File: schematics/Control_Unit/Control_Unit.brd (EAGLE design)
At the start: 49.8 x 49.8 mm, 282 parts, among them IC1 74HC174N, IC10 74HC74N, IC101 74HCT08N, IC102 74HC151N, IC103 74HC373N, IC104 74HCT08N, IC105 74HC151N, IC106 74HC151N, IC108 74HCT32N, IC109 74HCT08N, IC11 74HC74N, IC110 74HCT32N, IC111 74HC151N, IC112 74HCT32N, IC113 74HC151N, IC114 74HC151N, IC115 74HC151N, IC116 74HC373N, IC117 74HC74N, IC12 74AC08N, IC124 74HCT32N, IC125 74HCT08N, IC126 74AC157N, IC127 74HCT08N, IC128 74AC08N, IC129 74AC08N, IC13 74AC08N, IC130 74HCT04N, IC133 74HCT04N, IC134 74HCT08N, IC135 74HCT08N, IC136 74HCT08N, IC14 74HC74N, IC141 74HCT32N, IC15 74HC74N, IC16 74AC08N, IC164 74HC174N, IC165 74HC174N, IC166 74HC174N, IC167 74HC174N, IC168 74HCT32N, IC169 74HCT32N, IC17 74HCT32N, IC172 74HCT32N, IC173 74HCT32N, IC175 74HC193N, IC176 74HC193N, IC177 74HC193N, IC178 74HC193N, IC179 74HC193N, IC18 74AC08N, IC180 74HC193N, IC181 74HC193N, IC182 74HC193N, IC19 74AC08N, IC190 74HCT32N, IC191 74HCT32N, IC2 74HC174N, IC20 74AC08N, IC21 74AC08N, IC22 74HCT32N, IC23 74HCT08N, IC24 74HCT08N, IC25 74HCT32N, IC26 74HCT08N, IC27 74HCT08N, IC28 74HCT08N, IC29 74HCT32N, IC3 74HC151N, IC30 74HCT08N, IC31 74HC74N, IC32 74HCT32N, IC33 74HCT32N, IC34 74HCT08N, IC35 74HCT04N, IC36 74HCT32N, IC38 74HCT08N, IC39 74HCT08N, IC4 74HC174N, IC40 74ACT157N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

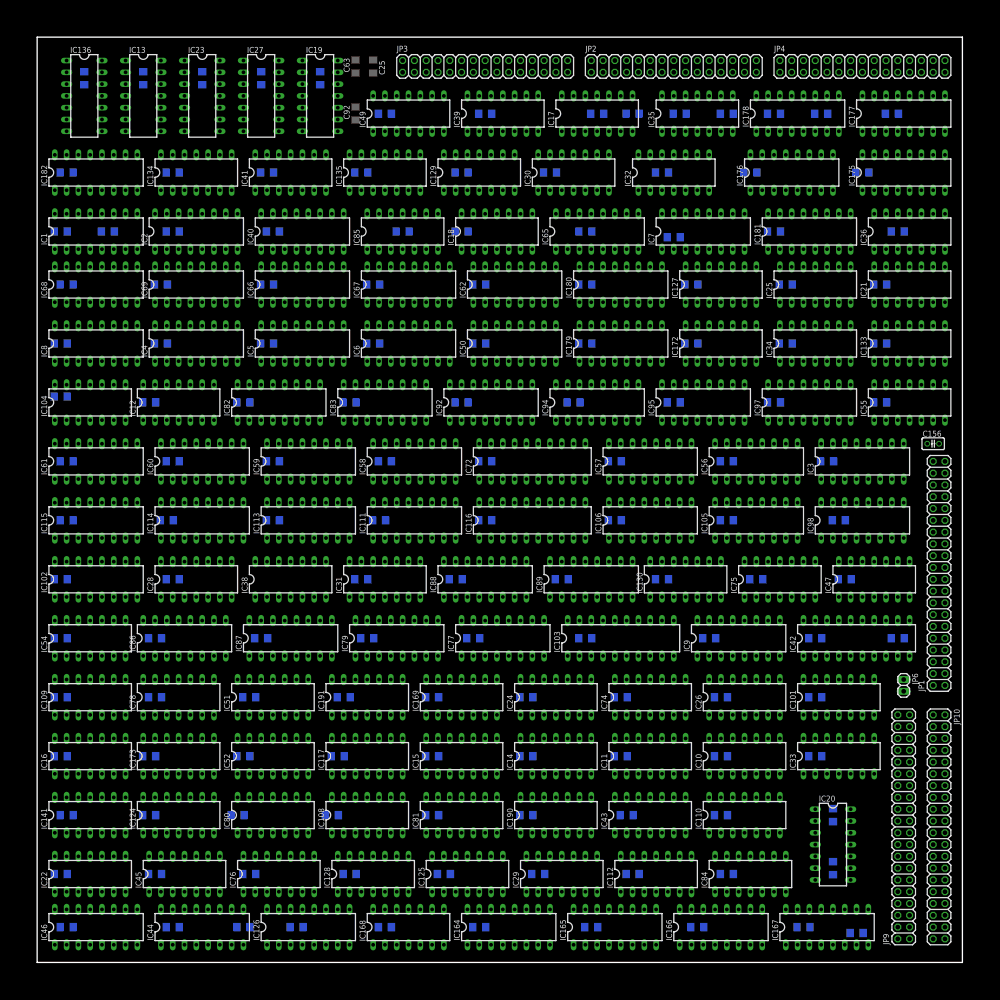
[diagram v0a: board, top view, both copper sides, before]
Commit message: remove 2 more chips
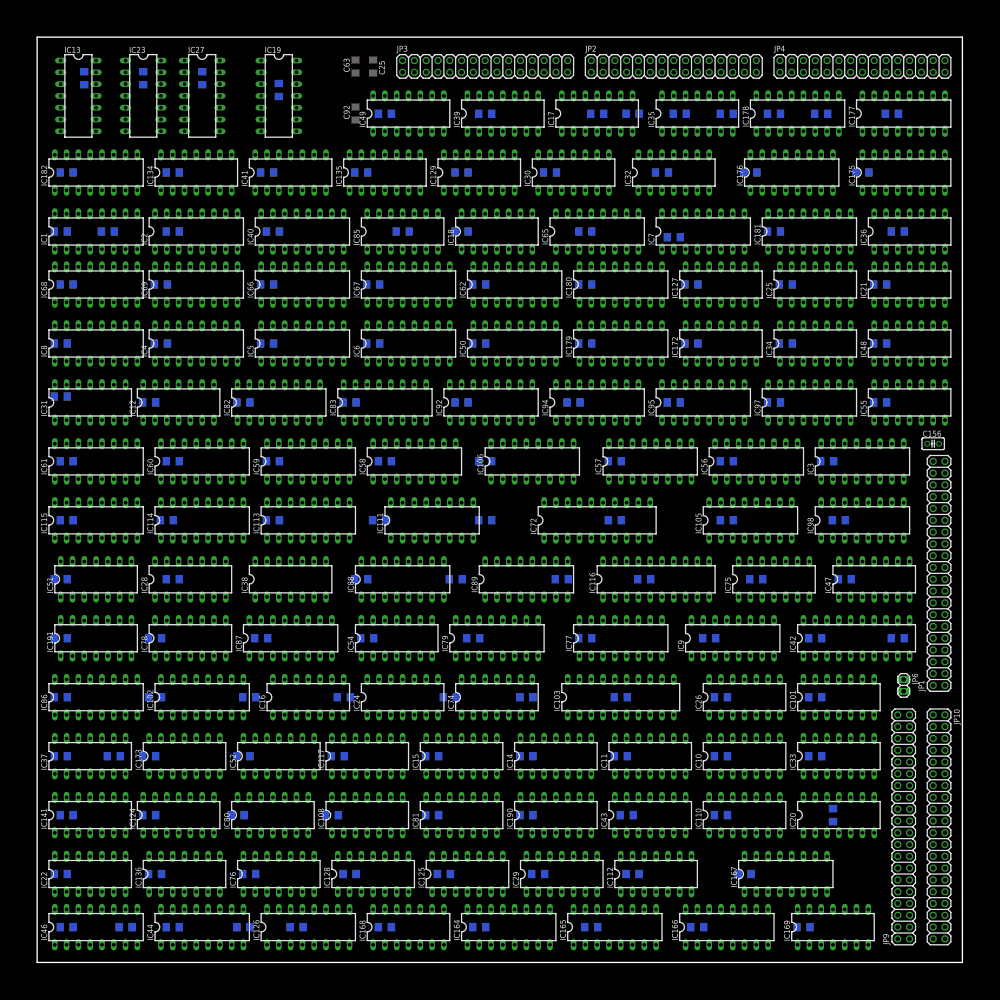
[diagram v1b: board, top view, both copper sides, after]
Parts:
- removed C128: (no value), rcl:C1206
- removed IC104, IC109: 74HCT08N, 74xx-eu:DIL14
- removed IC130: 74HCT04N, 74xx-eu:DIL14
- removed IC45, IC84: 74HCT32N, 74xx-eu:DIL14
- added IC37: 74ACT02N, 74xx-eu:DIL14
- IC31: value 74HC74N -> 74HCT00N
- IC48: value 74HCT04N -> 74ACT02N
- moved IC136 42.3 mm to (7.94, 4.76), turned to 0 degrees
- moved C78 41.1 mm to (4.13, 11.1)
- moved C102 38.2 mm to (4.76, 1.91), turned to 180 degrees
- moved IC169 23.5 mm to (42.9, 1.91)
- moved IC31 18.5 mm to (2.86, 30.2)
- moved IC54 16.5 mm to (19.4, 17.5)
- moved IC191 14.9 mm to (3.17, 17.5)
- moved IC16 12.2 mm to (14.6, 14.3)
- moved IC51 11.4 mm to (3.17, 20.6)
- moved IC102 8.54 mm to (8.89, 14.3)
- moved IC24 8.26 mm to (19.7, 14.3)
- moved IC74 8.26 mm to (24.8, 14.3)
- moved IC116 7.38 mm to (33.3, 20.6)
- moved IC106 7.10 mm to (26.7, 27.0)
- moved IC77 6.35 mm to (31.4, 17.5)
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- renumbered IC133 to IC48
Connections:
- net N$73 renamed PC_HIGH_LOAD_INPUT_NOT
- net PC_HIGH_LOAD_INPUT renamed N$163
- removed net ALU_CARRY_OUT_: IC31.12, IC31.2, JP9.32
- removed net DASSDADASDASDA: IC1.1, IC179.14, IC180.14, IC181.14, IC182.14, IC2.1, IC2.11, IC2.13, IC2.14, IC2.6, IC36.3, IC4.1, IC5.1, IC5.11, IC5.13, IC5.14, IC5.6, IC50.1, IC50.11, IC50.13, IC50.14, IC50.6, IC6.1, IC62.1, IC65.1, IC65.11, IC65.13, IC65.14, IC65.6, IC66.1, IC67.1, IC67.11, IC67.13, IC67.14, IC67.6, IC68.1, IC69.1, IC69.11, IC69.13, IC69.14, IC69.6, IC7.1, IC8.1, IC8.11, IC8.13, IC8.14, IC8.6, IC82.14, IC83.14, IC92.1, IC94.1, IC94.11, IC94.13, IC94.14, IC94.6, IC95.1, IC97.1, IC97.11, IC97.13, IC97.14, IC97.6
- removed net LR_H_LOAD_INPUT: IC48.13, IC84.11
- removed net LR_L_LOAD_INPUT: IC48.11, IC84.8
- removed net N$101: IC44.10, IC45.3
- removed net N$129: IC109.10, IC130.10
- removed net N$130: IC23.3, IC47.13
- removed net N$131: IC24.8, IC47.11
- removed net N$135: IC31.11, IC33.11, IC35.11
- removed net N$137: IC101.13, IC101.3
- removed net N$153: IC127.2, IC127.6
- removed net N$163 (its old number): IC84.3, IC84.5
- removed net N$167: IC48.12, IC95.9, IC97.9
- removed net N$234: IC48.10, IC92.9, IC94.9
- removed net N$249: IC141.10, IC141.11
- removed net N$267: IC109.6, IC116.11, IC48.1
- removed net N$268: IC109.1, IC49.11
- removed net N$269: IC116.1, IC48.2
- removed net N$69: IC35.6, JP3.22
- removed net N$7: IC127.3, IC130.13
- removed net N$72: IC1.9, IC2.9, IC48.6
- removed net N$99: IC35.8, JP2.22
- removed net PC_LOW_LOAD_INPUT: IC48.9, IC84.6
- removed net PTR_L_LOAD_INPUT: IC169.8, IC48.5
- removed net STATE_4/CYCL_10: IC10.2, IC101.1, IC117.9, IC127.4, JP1.38
- removed net UNNAME: IC179.11, IC180.11, IC48.8
- new net LR_H_LOAD_INPUT_NOT: IC37.13, IC95.9, IC97.9
- new net LR_L_LOAD_INPUT_NOT: IC37.4, IC92.9, IC94.9
- new net N$44: IC34.13, IC35.10
- new net N$52: IC116.1, IC49.11
- new net N$67: IC35.6, IC36.1
- new net PC_LOW_LOAD_INPUT_NOT: IC179.11, IC180.11, IC48.1
- new net PTR_L_LOAD_INPUT_NOT: IC1.9, IC2.9, IC37.10
- new net WRITE_PC_H/WRITE_PC_L_DBUS_SAVE_LR: IC141.10, IC141.11, IC44.10
- net !CLR_CARRY_BIT: now also IC117.13; no longer IC31.1
- net !REGISTER_RESET: now also IC1.1, IC179.14, IC180.14, IC181.14, IC182.14, IC2.1, IC2.11, IC2.13, IC2.14, IC2.6, IC4.1, IC5.1, IC5.11, IC5.13, IC5.14, IC5.6, IC50.1, IC50.11, IC50.13, IC50.14, IC50.6, IC6.1, IC62.1, IC65.1, IC65.11, IC65.13, IC65.14, IC65.6, IC66.1, IC67.1, IC67.11, IC67.13, IC67.14, IC67.6, IC68.1, IC69.1, IC69.11, IC69.13, IC69.14, IC69.6, IC7.1, IC8.1, IC8.11, IC8.13, IC8.14, IC8.6, IC82.14, IC83.14, IC92.1, IC94.1, IC94.11, IC94.13, IC94.14, IC94.6, IC95.1, IC97.1, IC97.11, IC97.13, IC97.14, IC97.6; no longer IC36.1
- net !RING_CNTR_RESET: no longer IC117.13
- net !SET_CARRY_BIT: now also IC117.10; no longer IC31.4
- net ADRR_15: now also IC25.9, IC35.5; no longer IC34.12, IC35.13
- net ALU_CARRY_BIT: now also IC117.9; no longer IC31.5
- net ALU_CARRY_OUT: now also IC117.12, IC31.12, JP9.32; no longer IC127.1, IC31.9
- net CLR_NOT_OE/CLR_NOT_CS_CYCL_0: now also IC48.8; no longer IC85.5
- net CONNECT_PTR_TO_ABUS/CLR_NOT_OE_LDR: now also IC48.9; no longer IC85.6
- net CYCL_1: now also JP1.22; no longer JP1.20
- net CYCL_3: now also JP1.26; no longer JP1.24
- net CYCL_4: now also IC127.1, JP1.28; no longer IC104.4, JP1.26
- net DATA_BUS_ENABLE_LATCH: now also IC101.3, IC35.9; no longer IC109.3, IC130.1
- net FILL_LR_H_SAVE_LR: now also IC37.11; no longer IC84.12
- net FILL_LR_L_SAVE_LR: now also IC37.5; no longer IC84.9
- net FILL_PC_L_JMP_O: now also IC101.13, IC80.9; no longer IC84.1
- net FILL_PC_L_RET: now also IC80.10; no longer IC84.2
- net FILL_PTR_H_SET_PTR: now also IC37.3; no longer IC169.5
- net FILL_PTR_L_PTR_ADD: now also IC24.8, IC31.13; no longer IC104.8
- net FILL_PTR_L_SET_PTR: now also IC37.9; no longer IC169.10
- net FILL_REGISTER_ALU/ALU_TO_DBUS: now also IC117.11, IC54.8; no longer IC31.3, IC33.12
- net GND: now also IC37.7, JP1.16, JP1.20; no longer C128.2, IC104.7, IC109.7, IC130.7, IC36.2, IC45.7, IC84.7
- net INPUT_REG0: now also IC31.4; no longer IC28.4
- net INPUT_REG_IS_NOT_OUTPUT_REG: now also IC48.12; no longer IC36.5
- net IR_DATA_OUT_7: now also IC47.11, IC49.10; no longer IC130.5, IC130.9
- net IR_LOAD_INPUT: now also IC127.3; no longer IC104.6
- net LATCH_ALU_INPUT_B_PTR_ADD: now also IC23.3; no longer IC104.11
- net LR_H_LOAD_INPUT_TABLE_1: now also IC37.12; no longer IC84.13
- net LR_L_LOAD_INPUT_TABLE_1: now also IC37.6; no longer IC84.10
- net MEM_NOT_CE: now also IC25.10, IC36.2, IC85.4; no longer IC17.8, IC34.10, IC34.13
- net MEM_NOT_OE: now also IC48.10; no longer IC85.4
- net N$12: now also IC116.11, IC34.8, IC49.12; no longer IC49.8, IC54.8
- net N$121: now also IC169.9; no longer IC25.9
- net N$126: now also IC85.5; no longer IC17.9
- net N$128: now also IC49.8; no longer IC130.8
- net N$132: no longer IC101.2
- net N$14: now also IC54.10; no longer IC35.10
- net N$147: now also IC54.9; no longer IC33.13
- net N$149: now also IC31.6, IC47.13; no longer IC130.4
- net N$159: now also IC31.11; no longer IC130.12
- net N$164: now also IC47.10; no longer IC130.6
- net N$171: now also IC17.8; no longer IC45.11
- net N$194: now also IC127.6; no longer IC109.11
- net N$200: now also IC85.6; no longer IC17.10
- net N$203: now also IC169.6; no longer IC54.10
- net N$21: now also IC169.4; no longer IC49.10
- net N$217: now also IC48.11; no longer IC36.4
- net N$219: now also IC34.11; no longer IC109.8
- net N$22: now also IC47.12; no longer IC130.3, IC28.6
- net N$227: now also IC169.5, IC48.13; no longer IC36.6, IC54.9
- net N$252: now also IC169.10; no longer IC25.10
- net N$266: now also IC101.2, IC169.8, IC34.10; no longer IC109.2, IC109.5, IC25.8
- net N$31: now also IC36.3, JP3.22; no longer IC34.11, IC35.5
- net N$32: now also IC36.6, IC48.2; no longer IC45.6, IC84.4
- net N$33: now also IC48.6; no longer IC80.10
- net N$47: now also IC33.11; no longer IC45.8
- net N$68: now also IC101.1; no longer IC34.9
- net N$70: now also IC25.8, JP2.22; no longer IC34.8, IC35.9
- net OPCODE_5: now also IC127.4, IC35.11; no longer IC109.12, IC130.11
- net OPCODE_LOAD_INPUT/CYCL_2: now also JP1.24; no longer JP1.22
- net OUTPUT_REG0_JMP: now also IC31.5; no longer IC28.5
- net PC_COUNT_UP_FETCH2/CYCL_5: now also JP1.30; no longer JP1.28
- net PC_HIGH_LOAD_INPUT_JMP: now also IC48.5; no longer IC80.9
- net PC_LOW_LOAD_INPUT_JMP: now also IC36.4; no longer IC45.4
- net PC_L_LOAD_INPUT_TABLE_1: now also IC36.5; no longer IC45.5
- net POP: now also IC31.2; no longer IC24.10
- net PTR_ADD: now also IC23.2, IC24.10, IC28.5; no longer IC104.10, IC104.13, IC104.2, IC127.5
- net PTR_H_LOAD_INPUT_NOT: now also IC37.1; no longer IC169.6
- net PUSH: now also IC31.10; no longer IC23.2
- net REGISTER_OUTPUT_SEL_3: now also IC34.9, IC35.13; no longer IC109.4, IC49.13
- net REGS_OUTPUT_TO_DATABUS_ENABLE: now also IC35.8; no longer IC130.2
- net RING_CNTR_CLOCK: no longer IC117.11
- net SAVE_LR/RET: now also IC127.5, IC34.12; no longer IC109.13, IC109.9
- net SECOND_LATCH_SELECT: now also IC33.12; no longer IC45.9
- net SP_COUNT_DOWN: now also IC31.3; no longer IC47.10
- net SP_COUNT_UP: now also IC31.8; no longer IC47.12
- net STATE_0/CYCL_6: now also IC31.9, JP1.32; no longer IC23.1, JP1.30
- net STATE_1/CYCL_7: now also IC23.1, JP1.34; no longer IC104.12, JP1.32
- net STATE_2/CYCL_8: now also IC28.4, JP1.36; no longer IC104.1, JP1.34
- net STATE_3/CYCL_9: now also IC10.2, IC31.1, JP1.38; no longer IC104.9, IC117.12, JP1.36
- net TABLE_1_INPUT_PTR_HIGH: now also IC37.2; no longer IC169.4
- net TABLE_1_INPUT_PTR_L: now also IC37.8; no longer IC169.9
- net TWO_BYTE_CMD: now also IC127.2; no longer IC104.5
- net VCC: now also IC37.14, IC49.13; no longer C128.1, IC104.14, IC109.14, IC117.10, IC130.14, IC31.10, IC31.13, IC45.14, IC49.12, IC84.14
- net WRITE_LR_H_DBUS_RET: now also IC17.9; no longer IC45.12
- net WRITE_PC_H_DBUS_SAVE_LR: no longer IC45.2
- net WRITE_PC_L_DBUS_SAVE_LR: now also IC17.10; no longer IC45.1, IC45.13
- net WRITE_PTR_L_TO_DBUS_PTR_ADD: now also IC33.13; no longer IC45.10
- net WRITE_REGB_TO_DBUS_PTR_ADD: now also IC28.6; no longer IC104.3

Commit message: add UI board schematic
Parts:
- removed C25: (no value), rcl:C1206
- removed IC164, IC165, IC166, IC167: 74HC174N, 74xx-eu:DIL16
- added IC45, IC53: 74HC373N, 74xx-eu:DIL20
- IC40: value 74ACT157N -> 74HCT08N; device 74xx-eu:DIL16 -> 74xx-eu:DIL14
- moved IC169 54.5 mm to (11.7, 46.7), turned to 270 degrees
- moved IC168 23.8 mm to (34.6, 20.6)
- moved IC112 16.3 mm to (29.5, 20.6)
- moved IC89 12.5 mm to (14.3, 17.5)
- moved IC77 9.14 mm to (40.0, 14.3)
- moved IC101 8.57 mm to (34.6, 14.3)
- moved C36 8.26 mm to (34.6, 14.3)
- moved C110 8.26 mm to (14.6, 14.3)
- moved C53 8.26 mm to (9.53, 14.3)
- moved C105 8.25 mm to (24.8, 14.3)
- moved C142 8.25 mm to (19.7, 14.3)
- moved C99 8.25 mm to (30.5, 14.3)
- moved IC116 7.38 mm to (26.7, 23.8)
- moved IC106 7.10 mm to (33.0, 23.8)
- moved IC26 6.54 mm to (32.4, 17.5)
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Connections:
- net !REGISTER_RESET: no longer IC164.1, IC165.1, IC165.11, IC165.13, IC165.14, IC165.6, IC166.1, IC167.1, IC167.11, IC167.13, IC167.14, IC167.6
- net ALU_CARRY_BIT: now also IC40.1; no longer IC40.3
- net ALU_CARRY_IN: now also IC40.3; no longer IC40.4
- net DATA0: now also IC45.3, IC53.3; no longer IC164.3, IC166.3
- net DATA1: now also IC45.4, IC53.4; no longer IC164.4, IC166.4
- net DATA2: now also IC45.7, IC53.7; no longer IC164.6, IC166.6
- net DATA3: now also IC45.8, IC53.8; no longer IC164.11, IC166.11
- net DATA4: now also IC45.13, IC53.13; no longer IC164.13, IC166.13
- net DATA5: now also IC45.14; no longer IC164.14
- net DATA6: now also IC45.17, IC53.14, IC53.17; no longer IC165.3, IC166.14, IC167.3
- net DATA7: now also IC45.18, IC53.18; no longer IC165.4, IC167.4
- net GND: now also IC40.7, IC45.1, IC45.10, IC53.1, IC53.10; no longer C25.2, IC164.8, IC165.8, IC166.8, IC167.8, IC40.1, IC40.10, IC40.11, IC40.13, IC40.14, IC40.2, IC40.5, IC40.6, IC40.8
- net IO_OUTPUT1_0: now also IC45.2; no longer IC164.2
- net IO_OUTPUT1_1: now also IC45.5; no longer IC164.5
- net IO_OUTPUT1_2: now also IC45.6; no longer IC164.7
- net IO_OUTPUT1_3: now also IC45.9; no longer IC164.10
- net IO_OUTPUT1_4: now also IC45.12; no longer IC164.12
- net IO_OUTPUT1_5: now also IC45.15; no longer IC164.15
- net IO_OUTPUT1_6: now also IC45.16; no longer IC165.2
- net IO_OUTPUT1_7: now also IC45.19; no longer IC165.5
- net IO_OUTPUT2_0: now also IC53.2; no longer IC166.2
- net IO_OUTPUT2_1: now also IC53.5; no longer IC166.5
- net IO_OUTPUT2_2: now also IC53.6; no longer IC166.7
- net IO_OUTPUT2_3: now also IC53.9; no longer IC166.10
- net IO_OUTPUT2_4: now also IC53.12; no longer IC166.12
- net IO_OUTPUT2_5: now also IC53.15; no longer IC166.15
- net IO_OUTPUT2_6: now also IC53.16; no longer IC167.2
- net IO_OUTPUT2_7: now also IC53.19; no longer IC167.5
- net IO_OUTPUT_REG_1_LOAD_INPUT: now also IC45.11; no longer IC164.9, IC165.9
- net IO_OUTPUT_REG_2_LOAD_INPUT: now also IC53.11; no longer IC166.9, IC167.9
- net SELECT_CARRY_BIT: now also IC40.2; no longer IC40.15
- net VCC: now also IC40.14, IC45.20, IC53.20; no longer C25.1, IC164.16, IC165.16, IC166.16, IC167.16, IC40.16
